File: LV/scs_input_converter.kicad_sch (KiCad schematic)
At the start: 4 parts, among them Q7 SS8050, U11 TLV172IDCK, U14 74AHC1G08, U2 MCP6562

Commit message: Finished V1.0 of Schematic and PCB
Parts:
- removed Q7: SS8050, Package_TO_SOT_SMD:SOT-23, symbol Transistor_BJT:SS8050
- removed U11: TLV172IDCK, Package_TO_SOT_THT:TO-5-8_PD5.08_Window, symbol Amplifier_Operational:TLV172IDCK
- added U9: TLV172IDCK, Package_TO_SOT_SMD:SOT-353_SC-70-5, symbol Amplifier_Operational:TLV172IDCK
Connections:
- net +12V: now also U9.5 (V+)
- net GND: now also U9.2 (V-)
- net Input: now also U9.1 (+)
- net at U2.2 (-), U2.5 (+): now also U9.3 (-), U9.4
- net +1V renamed +3.5V
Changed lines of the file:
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@@
 		)
 	)
-	(hierarchical_label "+1V"
+	(hierarchical_label "+3.5V"
 		(shape input)
 		(at 109.22 87.63 180)
@@
 		)
 		(instances
+			(project "AMS-IMD-RST"
+				(path "/7d9bad3e-6cf2-4a61-8644-78bfbb2e310d/51faaed0-0471-499a-9315-dcb7d14024a1"
+					(reference "U2")
+					(unit 1)
+				)
+				(path "/7d9bad3e-6cf2-4a61-8644-78bfbb2e310d/69a2ded7-52c2-4d2a-9dd8-18f6752f1aaa"
+					(reference "U6")
+					(unit 1)
+				)
+				(path "/7d9bad3e-6cf2-4a61-8644-78bfbb2e310d/d57cec0e-b69b-4e9e-b272-7d17425fc8d9"
+					(reference "U5")
+					(unit 1)
+				)
+			)
+			(project "scs_input_converter"
+				(path "/8b045c68-f2ee-46b4-b98d-dfb029bb17f8"
+					(reference "U?")
+					(unit 1)
+				)
+			)
+		)
+	)
+	(symbol
+		(lib_id "Amplifier_Operational:TLV172IDCK")
+		(at 90.17 64.77 0)
+		(unit 1)
+		(exclude_from_sim no)
+		(in_bom yes)
+		(on_board yes)
+		(dnp no)
+		(fields_autoplaced yes)
+		(property "Reference" "U9"
+			(at 105.41 58.3498 0)
+			(effects
+				(font
+					(size 1.27 1.27)
+				)
+			)
+		)
+		(property "Value" "TLV172IDCK"
+			(at 105.41 60.8898 0)
+			(effects
+				(font
+					(size 1.27 1.27)
+				)
+			)
+		)
+		(property "Footprint" "Package_TO_SOT_SMD:SOT-353_SC-70-5"
+			(at 95.25 64.77 0)
+			(effects
+				(font
+					(size 1.27 1.27)
+				)
+				(hide yes)
+			)
+		)
+		(property "Datasheet" "http://www.ti.com/lit/ds/symlink/tlv172.pdf"
+			(at 90.17 64.77 0)
+			(effects
+				(font
+					(size 1.27 1.27)
+				)
+				(hide yes)
+			)
+		)
+		(property "Description" "Low-power Operational Amplifier, SOT-353"
+			(at 90.17 64.77 0)
+			(effects
+				(font
+					(size 1.27 1.27)
+				)
+				(hide yes)
+			)
+		)
+		(pin "2"
+		)
+		(pin "4"
+		)
+		(pin "5"
+		)
+		(pin "1"
+		)
+		(pin "3"
+		)
+		(instances
 			(project ""
 				(path "/7d9bad3e-6cf2-4a61-8644-78bfbb2e310d/51faaed0-0471-499a-9315-dcb7d14024a1"
-					(reference "U2")
+					(reference "U9")
 					(unit 1)
 				)
 				(path "/7d9bad3e-6cf2-4a61-8644-78bfbb2e310d/69a2ded7-52c2-4d2a-9dd8-18f6752f1aaa"
-					(reference "U6")
+					(reference "U17")
 					(unit 1)
 				)
 				(path "/7d9bad3e-6cf2-4a61-8644-78bfbb2e310d/d57cec0e-b69b-4e9e-b272-7d17425fc8d9"
-					(reference "U5")
+					(reference "U10")
 					(unit 1)
 				)
@@
 		)
 		(instances
-			(project ""
+			(project "AMS-IMD-RST"
 				(path "/7d9bad3e-6cf2-4a61-8644-78bfbb2e310d/51faaed0-0471-499a-9315-dcb7d14024a1"
 					(reference "U2")
@@
 					(reference "U5")
 					(unit 2)
+				)
+			)
+			(project "scs_input_converter"
+				(path "/8b045c68-f2ee-46b4-b98d-dfb029bb17f8"
+					(reference "U?")
+					(unit 1)
 				)
 			)
@@
 		)
 		(instances
-			(project ""
+			(project "AMS-IMD-RST"
 				(path "/7d9bad3e-6cf2-4a61-8644-78bfbb2e310d/51faaed0-0471-499a-9315-dcb7d14024a1"
 					(reference "U14")
@@
 				)
 			)
-		)
-	)
-	(symbol
-		(lib_id "Transistor_BJT:SS8050")
-		(at 87.63 83.82 0)
-		(unit 1)
-		(exclude_from_sim no)
-		(in_bom yes)
-		(on_board yes)
-		(dnp no)
-		(fields_autoplaced yes)
-		(property "Reference" "Q7"
-			(at 92.71 82.5499 0)
-			(effects
-				(font
-					(size 1.27 1.27)
-				)
-				(justify left)
-			)
-		)
-		(property "Value" "SS8050"
-			(at 92.71 85.0899 0)
-			(effects
-				(font
-					(size 1.27 1.27)
-				)
-				(justify left)
-			)
-		)
-		(property "Footprint" "Package_TO_SOT_SMD:SOT-23"
-			(at 92.71 91.186 0)
-			(effects
-				(font
-					(size 1.27 1.27)
-					(italic yes)
-				)
-				(justify left)
-				(hide yes)
-			)
-		)
-		(property "Datasheet" "http://www.secosgmbh.com/datasheet/products/SSMPTransistor/SOT-23/SS8050.pdf"
-			(at 92.71 88.646 0)
-			(effects
-				(font
-					(size 1.27 1.27)
-				)
-				(justify left)
-				(hide yes)
-			)
-		)
-		(property "Description" "General Purpose NPN Transistor, 1.5A Ic, 25V Vce, SOT-23"
-			(at 121.666 86.106 0)
-			(effects
-				(font
-					(size 1.27 1.27)
-				)
-				(hide yes)
-			)
-		)
-		(pin "2"
-		)
-		(pin "1"
-		)
-		(pin "3"
-		)
-		(instances
-			(project ""
-				(path "/7d9bad3e-6cf2-4a61-8644-78bfbb2e310d/51faaed0-0471-499a-9315-dcb7d14024a1"
-					(reference "Q7")
-					(unit 1)
-				)
-				(path "/7d9bad3e-6cf2-4a61-8644-78bfbb2e310d/69a2ded7-52c2-4d2a-9dd8-18f6752f1aaa"
-					(reference "Q9")
-					(unit 1)
-				)
-				(path "/7d9bad3e-6cf2-4a61-8644-78bfbb2e310d/d57cec0e-b69b-4e9e-b272-7d17425fc8d9"
-					(reference "Q8")
+			(project "scs_input_converter"
+				(path "/8b045c68-f2ee-46b4-b98d-dfb029bb17f8"
+					(reference "U?")
 					(unit 1)
 				)
@@
 		)
 		(instances
-			(project ""
+			(project "AMS-IMD-RST"
 				(path "/7d9bad3e-6cf2-4a61-8644-78bfbb2e310d/51faaed0-0471-499a-9315-dcb7d14024a1"
 					(reference "U2")
@@
 				)
 			)
-		)
-	)
-	(symbol
-		(lib_id "Amplifier_Operational:TLV172IDCK")
-		(at 90.17 64.77 0)
-		(unit 1)
-		(exclude_from_sim no)
-		(in_bom yes)
-		(on_board yes)
-		(dnp no)
-		(fields_autoplaced yes)
-		(property "Reference" "U11"
-			(at 105.41 58.3498 0)
-			(effects
-				(font
-					(size 1.27 1.27)
-				)
-			)
-		)
-		(property "Value" "TLV172IDCK"
-			(at 105.41 60.8898 0)
-			(effects
-				(font
-					(size 1.27 1.27)
-				)
-			)
-		)
-		(property "Footprint" "Package_TO_SOT_THT:TO-5-8_PD5.08_Window"
-			(at 95.25 64.77 0)
-			(effects
-				(font
-					(size 1.27 1.27)
-				)
-				(hide yes)
-			)
-		)
-		(property "Datasheet" "http://www.ti.com/lit/ds/symlink/tlv172.pdf"
-			(at 90.17 64.77 0)
-			(effects
-				(font
-					(size 1.27 1.27)
-				)
-				(hide yes)
-			)
-		)
-		(property "Description" "Low-power Operational Amplifier, SOT-353"
-			(at 90.17 64.77 0)
-			(effects
-				(font
-					(size 1.27 1.27)
-				)
-				(hide yes)
-			)
-		)
-		(pin "2"
-		)
-		(pin "4"
-		)
-		(pin "3"
-		)
-		(pin "5"
-		)
-		(pin "1"
-		)
-		(instances
-			(project ""
-				(path "/7d9bad3e-6cf2-4a61-8644-78bfbb2e310d/51faaed0-0471-499a-9315-dcb7d14024a1"
-					(reference "U11")
-					(unit 1)
-				)
-				(path "/7d9bad3e-6cf2-4a61-8644-78bfbb2e310d/69a2ded7-52c2-4d2a-9dd8-18f6752f1aaa"
-					(reference "U13")
-					(unit 1)
-				)
-				(path "/7d9bad3e-6cf2-4a61-8644-78bfbb2e310d/d57cec0e-b69b-4e9e-b272-7d17425fc8d9"
-					(reference "U12")
-					(unit 1)
-				)
+			(project "scs_input_converter"
+				(path "/8b045c68-f2ee-46b4-b98d-dfb029bb17f8"
+					(reference "U?")
+					(unit 1)
+				)

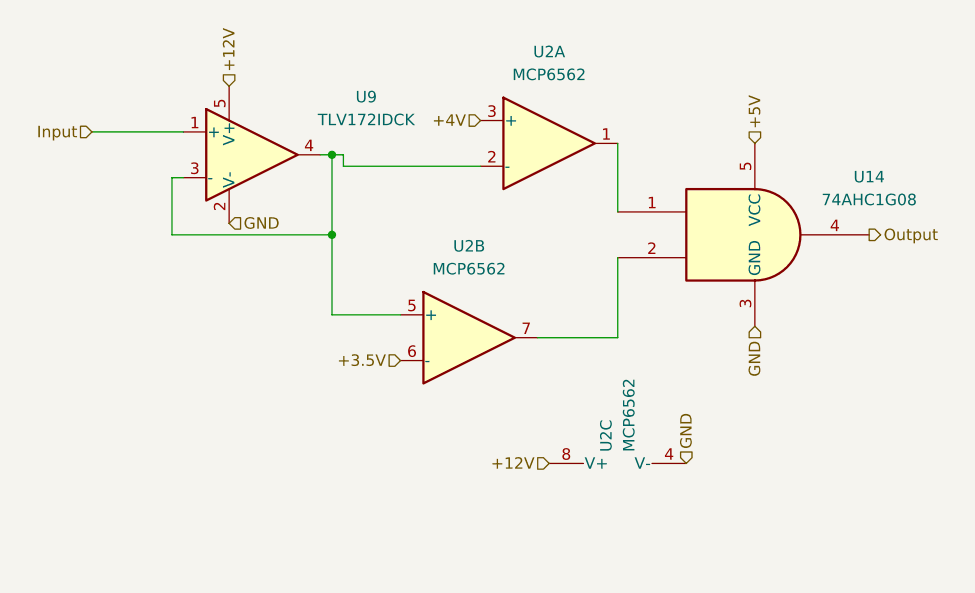
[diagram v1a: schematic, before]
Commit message: Added 2s lightning for T11.9.6 compliance
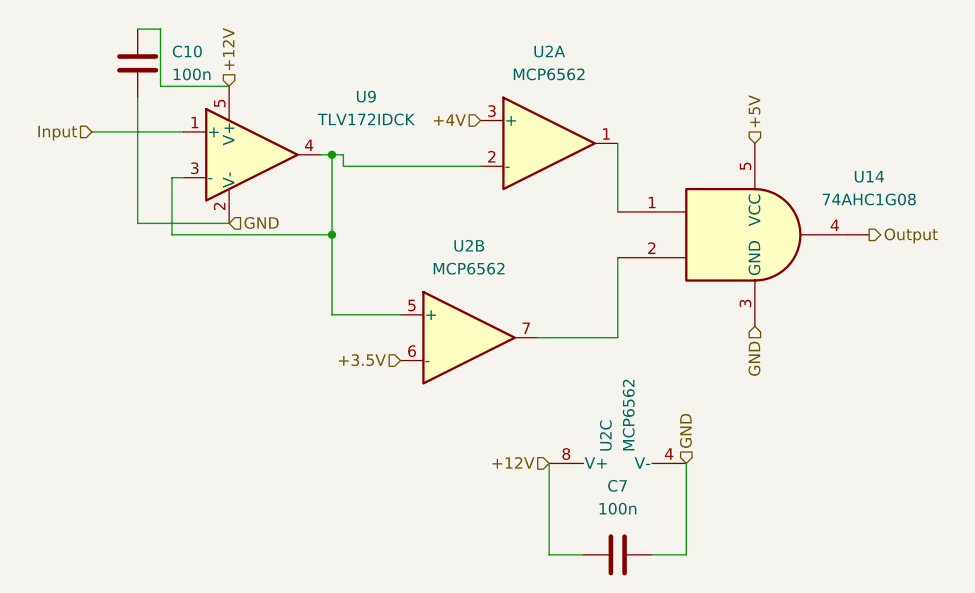
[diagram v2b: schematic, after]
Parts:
- added C10, C7: 100n, Capacitor_SMD:C_0805_2012Metric_Pad1.18x1.45mm_HandSolder, symbol Device:C
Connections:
- net +12V: now also C10.2, C7.1
- net GND: now also C10.1, C7.2
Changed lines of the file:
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@@
+	(wire
+		(pts
+			(xy 129.54 109.22) (xy 125.73 109.22)
+		)
+		(stroke
+			(width 0)
+			(type default)
+		)
+	)
 	(wire
 		(pts
@@
 	(wire
 		(pts
+			(xy 137.16 109.22) (xy 140.97 109.22)
+		)
+		(stroke
+			(width 0)
+			(type default)
+		)
+	)
+	(wire
+		(pts
 			(xy 124.46 85.09) (xy 133.35 85.09)
 		)
@@
 	(wire
 		(pts
+			(xy 82.55 50.8) (xy 82.55 57.15)
+		)
+		(stroke
+			(width 0)
+			(type default)
+		)
+	)
+	(wire
+		(pts
 			(xy 109.22 82.55) (xy 101.6 82.55)
 		)
@@
 	(wire
 		(pts
+			(xy 80.01 72.39) (xy 90.17 72.39)
+		)
+		(stroke
+			(width 0)
+			(type default)
+		)
+	)
+	(wire
+		(pts
 			(xy 133.35 85.09) (xy 133.35 76.2)
 		)
@@
 	(wire
 		(pts
+			(xy 140.97 109.22) (xy 140.97 99.06)
+		)
+		(stroke
+			(width 0)
+			(type default)
+		)
+	)
+	(wire
+		(pts
 			(xy 101.6 82.55) (xy 101.6 73.66)
 		)
@@
 	(wire
 		(pts
+			(xy 82.55 57.15) (xy 90.17 57.15)
+		)
+		(stroke
+			(width 0)
+			(type default)
+		)
+	)
+	(wire
+		(pts
 			(xy 83.82 73.66) (xy 101.6 73.66)
 		)
@@
 	(wire
 		(pts
+			(xy 125.73 99.06) (xy 125.73 109.22)
+		)
+		(stroke
+			(width 0)
+			(type default)
+		)
+	)
+	(wire
+		(pts
+			(xy 80.01 58.42) (xy 80.01 72.39)
+		)
+		(stroke
+			(width 0)
+			(type default)
+		)
+	)
+	(wire
+		(pts
 			(xy 83.82 67.31) (xy 83.82 73.66)
+		)
+		(stroke
+			(width 0)
+			(type default)
+		)
+	)
+	(wire
+		(pts
+			(xy 80.01 50.8) (xy 82.55 50.8)
 		)
 		(stroke
@@
 			)
 			(justify left)
+		)
+	)
+	(symbol
+		(lib_id "Device:C")
+		(at 133.35 109.22 90)
+		(unit 1)
+		(exclude_from_sim no)
+		(in_bom yes)
+		(on_board yes)
+		(dnp no)
+		(fields_autoplaced yes)
+		(property "Reference" "C7"
+			(at 133.35 101.6 90)
+			(effects
+				(font
+					(size 1.27 1.27)
+				)
+			)
+		)
+		(property "Value" "100n"
+			(at 133.35 104.14 90)
+			(effects
+				(font
+					(size 1.27 1.27)
+				)
+			)
+		)
+		(property "Footprint" "Capacitor_SMD:C_0805_2012Metric_Pad1.18x1.45mm_HandSolder"
+			(at 137.16 108.2548 0)
+			(effects
+				(font
+					(size 1.27 1.27)
+				)
+				(hide yes)
+			)
+		)
+		(property "Datasheet" "~"
+			(at 133.35 109.22 0)
+			(effects
+				(font
+					(size 1.27 1.27)
+				)
+				(hide yes)
+			)
+		)
+		(property "Description" "Unpolarized capacitor"
+			(at 133.35 109.22 0)
+			(effects
+				(font
+					(size 1.27 1.27)
+				)
+				(hide yes)
+			)
+		)
+		(pin "2"
+		)
+		(pin "1"
+		)
+		(instances
+			(project "AMS-IMD-RST"
+				(path "/7d9bad3e-6cf2-4a61-8644-78bfbb2e310d/51faaed0-0471-499a-9315-dcb7d14024a1"
+					(reference "C7")
+					(unit 1)
+				)
+				(path "/7d9bad3e-6cf2-4a61-8644-78bfbb2e310d/69a2ded7-52c2-4d2a-9dd8-18f6752f1aaa"
+					(reference "C9")
+					(unit 1)
+				)
+				(path "/7d9bad3e-6cf2-4a61-8644-78bfbb2e310d/d57cec0e-b69b-4e9e-b272-7d17425fc8d9"
+					(reference "C8")
+					(unit 1)
+				)
+			)
 		)
 	)
@@
 					(unit 1)
 				)
+			)
+		)
+	)
+	(symbol
+		(lib_id "Device:C")
+		(at 80.01 54.61 180)
+		(unit 1)
+		(exclude_from_sim no)
+		(in_bom yes)
+		(on_board yes)
+		(dnp no)
+		(fields_autoplaced yes)
+		(property "Reference" "C10"
+			(at 83.82 53.3399 0)
+			(effects
+				(font
+					(size 1.27 1.27)
+				)
+				(justify right)
+			)
+		)
+		(property "Value" "100n"
+			(at 83.82 55.8799 0)
+			(effects
+				(font
+					(size 1.27 1.27)
+				)
+				(justify right)
+			)
+		)
+		(property "Footprint" "Capacitor_SMD:C_0805_2012Metric_Pad1.18x1.45mm_HandSolder"
+			(at 79.0448 50.8 0)
+			(effects
+				(font
+					(size 1.27 1.27)
+				)
+				(hide yes)
+			)
+		)
+		(property "Datasheet" "~"
+			(at 80.01 54.61 0)
+			(effects
+				(font
+					(size 1.27 1.27)
+				)
+				(hide yes)
+			)
+		)
+		(property "Description" "Unpolarized capacitor"
+			(at 80.01 54.61 0)
+			(effects
+				(font
+					(size 1.27 1.27)
+				)
+				(hide yes)
+			)
+		)
+		(pin "2"
+		)
+		(pin "1"
+		)
+		(instances
+			(project "AMS-IMD-RST"
+				(path "/7d9bad3e-6cf2-4a61-8644-78bfbb2e310d/51faaed0-0471-499a-9315-dcb7d14024a1"
+					(reference "C10")
+					(unit 1)
+				)
+				(path "/7d9bad3e-6cf2-4a61-8644-78bfbb2e310d/69a2ded7-52c2-4d2a-9dd8-18f6752f1aaa"
+					(reference "C12")
+					(unit 1)
+				)
+				(path "/7d9bad3e-6cf2-4a61-8644-78bfbb2e310d/d57cec0e-b69b-4e9e-b272-7d17425fc8d9"
+					(reference "C11")
+					(unit 1)
+				)
